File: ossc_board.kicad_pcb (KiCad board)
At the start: 2 copper layers, 124.6 x 68.7 mm, 173 parts, among them J1 VGA, J10 CLK9, J11 CLK8, J12 CLK2, J13 SD_CLK, J21 I2C_BCK, J22 I2C_WS, J23 I2C_DATA, J24 I2C_MCLK, J4 HDMI_CONN, J5 5VDC_IN, P1 JTAG_CONN, SW1 SPST, SW2 SW_PUSH, SW3 SW_PUSH, U1 TVP7002PZP, U10 S25FL216K, U12 TLV70012, U13 TLV70025, U14 TLV70012, U15 TLV70018, U16 TLV70018, U2 EP4CE15E22, U3 IT6613, U4 SN74LVC2G17, U5 AP7361C, U6 TLV70033, U7 NCP703SN19T1G, U9 TLV70019, Y1 ACHL-27MHZ-EK

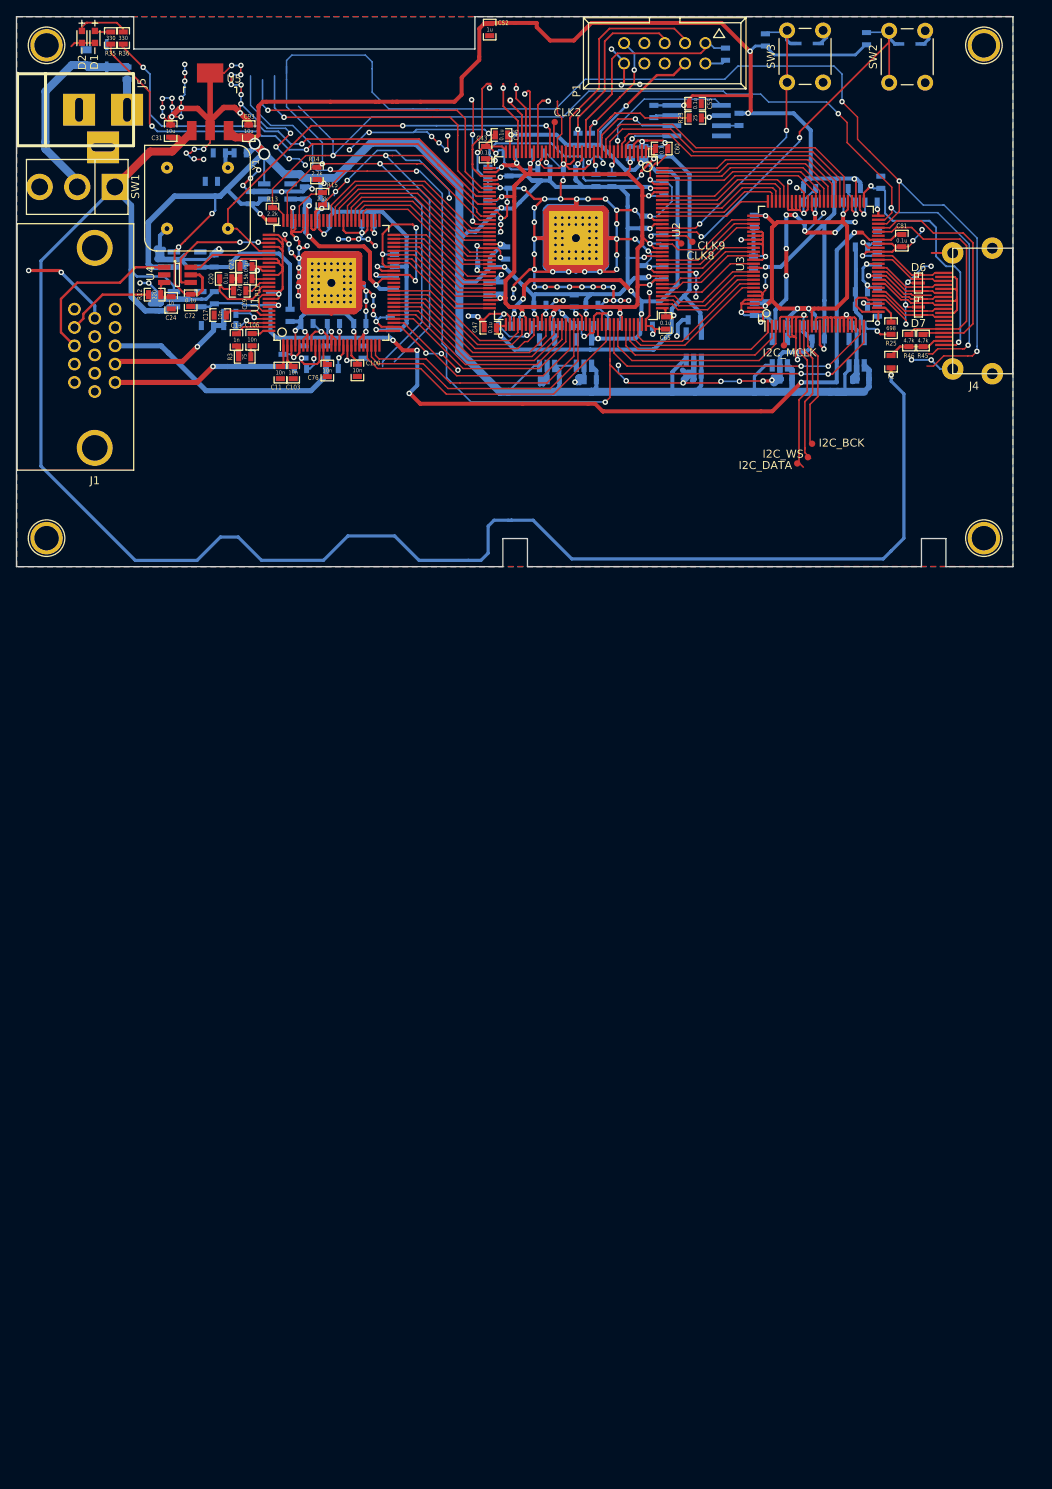
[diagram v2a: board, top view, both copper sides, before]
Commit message: NeXT Sound Box function (1st rev) (#1)
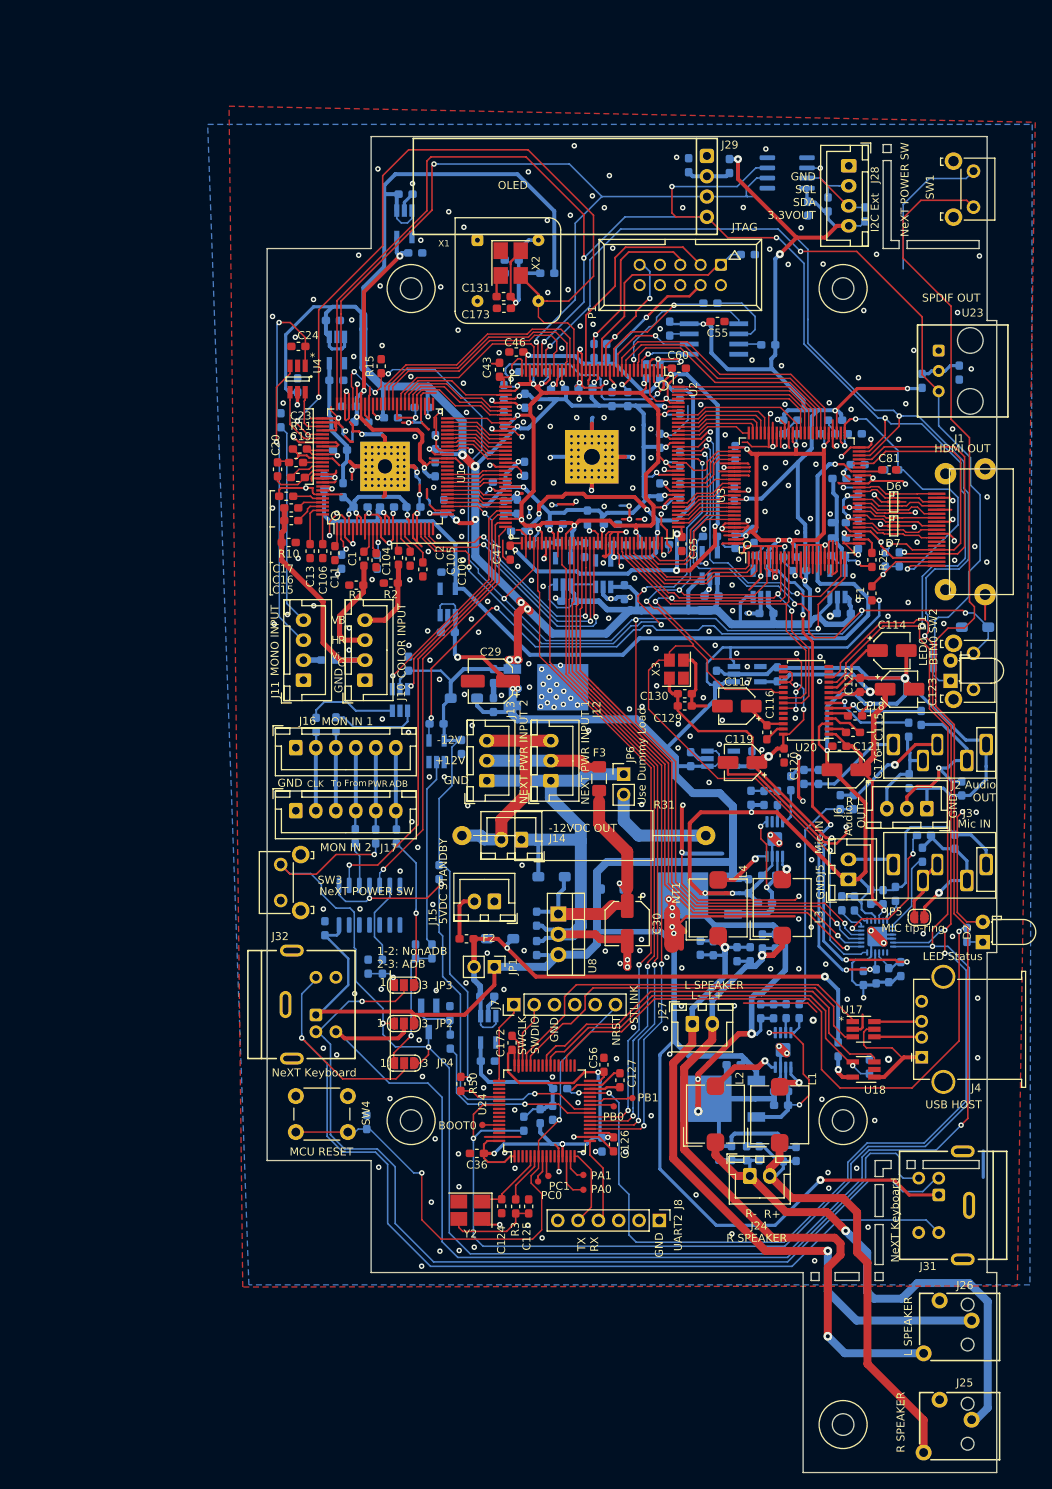
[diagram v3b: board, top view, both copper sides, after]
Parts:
- removed Y1: ACHL-27MHZ-EK, custom_components:ACHL-OSC
- added C102: 1u, Capacitor_SMD:C_0603_1608Metric_Pad1.05x0.95mm_HandSolder, B.Cu at (94.9, 99.7)
- added C111: 1u, Capacitor_SMD:C_0603_1608Metric_Pad1.05x0.95mm_HandSolder, B.Cu at (102.5, 99.2)
- added C112: 2200p (GRM1885C1H222JA01J), Capacitor_SMD:C_0603_1608Metric_Pad1.05x0.95mm_HandSolder, B.Cu at (125.5, 113.5)
- added C113: 2200p, Capacitor_SMD:C_0603_1608Metric_Pad1.05x0.95mm_HandSolder, B.Cu at (119.0, 112.6)
- added C114: 10u 16V, Capacitor_SMD:CP_Elec_4x4.5, F.Cu at (116.8, 96.3)
- added C115: 2.2u (GRM188R71A225KE15D), Capacitor_SMD:C_0603_1608Metric_Pad1.05x0.95mm_HandSolder, F.Cu at (111.9, 106.5)
- added C116: 0.1u, Capacitor_SMD:C_0603_1608Metric_Pad1.05x0.95mm_HandSolder, F.Cu at (101.2, 106.5)
- added C117: 10u 16V, Capacitor_SMD:CP_Elec_4x4.5, F.Cu at (97.4, 103.2)
- added C118: 2.2u, Capacitor_SMD:C_0603_1608Metric_Pad1.05x0.95mm_HandSolder, F.Cu at (112.2, 104.4)
- added C119: 10u 16V, Capacitor_SMD:CP_Elec_4x4.5, F.Cu at (98.1, 110.2)
- added C12: 1u, Capacitor_SMD:C_0603_1608Metric_Pad1.05x0.95mm_HandSolder, B.Cu at (125.2, 61.5)
- added C120: 0.1u, Capacitor_SMD:C_0603_1608Metric_Pad1.05x0.95mm_HandSolder, F.Cu at (103.3, 109.4)
- added C121: 0.1u, Capacitor_SMD:C_0603_1608Metric_Pad1.05x0.95mm_HandSolder, F.Cu at (110.2, 108.2)
- added C122: 0.1u, Capacitor_SMD:C_0603_1608Metric_Pad1.05x0.95mm_HandSolder, F.Cu at (112.8, 100.6)
- added C123: 10u 16V EEE-FK1C100AR or HB Series, Capacitor_SMD:CP_Elec_4x4.5, F.Cu at (117.8, 101.1)
- added C124: 10p, Capacitor_SMD:C_0603_1608Metric_Pad1.05x0.95mm_HandSolder, F.Cu at (68.0, 165.7)
- added C125: 10p, Capacitor_SMD:C_0603_1608Metric_Pad1.05x0.95mm_HandSolder, F.Cu at (71.4, 165.7)
- added C126: 0.01u, Capacitor_SMD:C_0603_1608Metric_Pad1.05x0.95mm_HandSolder, F.Cu at (82.0, 158.0)
- added C127: 2.2u, Capacitor_SMD:C_0603_1608Metric_Pad1.05x0.95mm_HandSolder, F.Cu at (82.8, 150.0)
- added C128: 0.1u, Capacitor_SMD:C_0603_1608Metric_Pad1.05x0.95mm_HandSolder, B.Cu at (51.2, 155.2)
- added C129: 1u, Capacitor_SMD:C_0603_1608Metric_Pad1.05x0.95mm_HandSolder, F.Cu at (90.9, 103.2)
- added C130: 0.01u, Capacitor_SMD:C_0603_1608Metric_Pad1.05x0.95mm_HandSolder, F.Cu at (90.9, 101.7)
- added C131: 0.01u, Capacitor_SMD:C_0603_1608Metric_Pad1.05x0.95mm_HandSolder, F.Cu at (68.3, 52.0)
- added C132: 0.1u, Capacitor_SMD:C_0603_1608Metric_Pad1.05x0.95mm_HandSolder, B.Cu at (63.0, 108.3)
- added C133: 0.1u, Capacitor_SMD:C_0603_1608Metric_Pad1.05x0.95mm_HandSolder, B.Cu at (45.9, 131.0)
- added C134: 0.1u, Capacitor_SMD:C_0603_1608Metric_Pad1.05x0.95mm_HandSolder, B.Cu at (116.4, 136.8)
- added C135: 0.1u, Capacitor_SMD:C_0603_1608Metric_Pad1.05x0.95mm_HandSolder, B.Cu at (115.7, 127.1)
- added C136: 1u, Capacitor_SMD:C_0603_1608Metric_Pad1.05x0.95mm_HandSolder, B.Cu at (114.2, 127.0)
- added C137: 0.1u, Capacitor_SMD:C_0603_1608Metric_Pad1.05x0.95mm_HandSolder, B.Cu at (113.2, 137.2)
- added C138: 1u, Capacitor_SMD:C_0603_1608Metric_Pad1.05x0.95mm_HandSolder, B.Cu at (114.8, 137.0)
- added C139: 1u, Capacitor_SMD:C_0603_1608Metric_Pad1.05x0.95mm_HandSolder, B.Cu at (120.6, 121.8)
- added C140: 1u, Capacitor_SMD:C_0603_1608Metric_Pad1.05x0.95mm_HandSolder, B.Cu at (117.2, 126.7)
- added C141: 1u, Capacitor_SMD:C_0603_1608Metric_Pad1.05x0.95mm_HandSolder, B.Cu at (124.7, 120.1)
- added C142: 0.1u, Capacitor_SMD:C_0603_1608Metric_Pad1.05x0.95mm_HandSolder, B.Cu at (112.1, 127.9)
- added C143: 0.1u, Capacitor_SMD:C_0603_1608Metric_Pad1.05x0.95mm_HandSolder, B.Cu at (110.5, 127.8)
- added C144: (220p), Capacitor_SMD:C_0603_1608Metric_Pad1.05x0.95mm_HandSolder, B.Cu at (57.3, 133.9)
- added C145: (220p), Capacitor_SMD:C_0603_1608Metric_Pad1.05x0.95mm_HandSolder, B.Cu at (51.3, 135.8)
- added C146: 2.2u, Capacitor_SMD:C_0603_1608Metric_Pad1.05x0.95mm_HandSolder, B.Cu at (102.9, 153.1)
- added C147: 1u, Capacitor_SMD:C_0603_1608Metric_Pad1.05x0.95mm_HandSolder, B.Cu at (98.9, 125.7)
- added C148: 0.1u, Capacitor_SMD:C_0603_1608Metric_Pad1.05x0.95mm_HandSolder, B.Cu at (102.9, 151.4)
- added C149: 2.2u, Capacitor_SMD:C_0603_1608Metric_Pad1.05x0.95mm_HandSolder, B.Cu at (112.0, 115.2)
- added C150: 0.1u, Capacitor_SMD:C_0603_1608Metric_Pad1.05x0.95mm_HandSolder, B.Cu at (110.4, 115.2)
- added C151: 0.1u, Capacitor_SMD:C_0603_1608Metric_Pad1.05x0.95mm_HandSolder, B.Cu at (103.2, 159.2)
- added C152: 1u, Capacitor_SMD:C_0603_1608Metric_Pad1.05x0.95mm_HandSolder, B.Cu at (104.8, 159.2)
- added C153: 0.1u, Capacitor_SMD:C_0603_1608Metric_Pad1.05x0.95mm_HandSolder, B.Cu at (102.0, 141.3)
- added C154: 0.1u, Capacitor_SMD:C_0603_1608Metric_Pad1.05x0.95mm_HandSolder, B.Cu at (96.7, 159.1)
- added C155: 1u, Capacitor_SMD:C_0603_1608Metric_Pad1.05x0.95mm_HandSolder, B.Cu at (95.2, 159.0)
- added C156: 1u, Capacitor_SMD:C_0603_1608Metric_Pad1.05x0.95mm_HandSolder, B.Cu at (100.2, 159.1)
- added C157: 2.2u, Capacitor_SMD:C_0603_1608Metric_Pad1.05x0.95mm_HandSolder, B.Cu at (100.4, 141.3)
- added C158: 0.1u, Capacitor_SMD:C_0603_1608Metric_Pad1.05x0.95mm_HandSolder, B.Cu at (98.6, 159.1)
- added C159: 2.2u, Capacitor_SMD:C_0603_1608Metric_Pad1.05x0.95mm_HandSolder, B.Cu at (101.5, 124.4)
- added C160: 1u, Capacitor_SMD:C_0603_1608Metric_Pad1.05x0.95mm_HandSolder, B.Cu at (97.0, 148.0)
- added C161: 0.1u, Capacitor_SMD:C_0603_1608Metric_Pad1.05x0.95mm_HandSolder, B.Cu at (100.9, 127.8)
- added C162: 2.2u, Capacitor_SMD:C_0603_1608Metric_Pad1.05x0.95mm_HandSolder, B.Cu at (107.6, 112.0)
- added C163: 0.1u, Capacitor_SMD:C_0603_1608Metric_Pad1.05x0.95mm_HandSolder, B.Cu at (105.8, 112.0)
- added C164: 0.1u, Capacitor_SMD:C_0603_1608Metric_Pad1.05x0.95mm_HandSolder, B.Cu at (100.6, 132.6)
- added C165: 1u, Capacitor_SMD:C_0603_1608Metric_Pad1.05x0.95mm_HandSolder, B.Cu at (102.3, 132.6)
- added C166: 0.1u, Capacitor_SMD:C_0603_1608Metric_Pad1.05x0.95mm_HandSolder, B.Cu at (100.8, 114.7)
- added C167: 0.1u, Capacitor_SMD:C_0603_1608Metric_Pad1.05x0.95mm_HandSolder, B.Cu at (92.8, 133.4)
- added C168: 1u, Capacitor_SMD:C_0603_1608Metric_Pad1.05x0.95mm_HandSolder, B.Cu at (94.5, 133.5)
- added C169: 1u, Capacitor_SMD:C_0603_1608Metric_Pad1.05x0.95mm_HandSolder, B.Cu at (97.4, 134.2)
- added C170: 2.2u, Capacitor_SMD:C_0603_1608Metric_Pad1.05x0.95mm_HandSolder, B.Cu at (99.2, 114.7)
- added C171: 0.1u, Capacitor_SMD:C_0603_1608Metric_Pad1.05x0.95mm_HandSolder, B.Cu at (99.1, 134.2)
- added C172: 0.1u, Capacitor_SMD:C_0603_1608Metric_Pad1.05x0.95mm_HandSolder, F.Cu at (69.3, 145.3)
- added C173: 1u, Capacitor_SMD:C_0603_1608Metric_Pad1.05x0.95mm_HandSolder, F.Cu at (68.3, 53.5)
- added C174: 0.1u, Capacitor_SMD:C_0603_1608Metric_Pad1.05x0.95mm_HandSolder, B.Cu at (106.3, 41.0)
- added C175: 0.1u, Capacitor_SMD:C_0603_1608Metric_Pad1.05x0.95mm_HandSolder, B.Cu at (91.4, 35.6)
- added C176: 10u 16V, Capacitor_SMD:CP_Elec_4x4.5, F.Cu at (111.1, 111.2)
- added C29: 47u, Capacitor_SMD:CP_Elec_5x5.3, F.Cu at (66.6, 100.1)
- added C3: 1u (GRT188R61H105KE13D), Capacitor_SMD:C_0603_1608Metric_Pad1.05x0.95mm_HandSolder, B.Cu at (66.2, 139.5)
- added C30: 47u (EEE-HBC470UAR), Capacitor_SMD:CP_Elec_5x5.3, F.Cu at (83.7, 130.4)
- added C36: 0.01u, Capacitor_SMD:C_0603_1608Metric_Pad1.05x0.95mm_HandSolder, F.Cu at (64.9, 159.1)
- added C4: 1u, Capacitor_SMD:C_0603_1608Metric_Pad1.05x0.95mm_HandSolder, B.Cu at (66.3, 147.6)
- added C5: 1u, Capacitor_SMD:C_0603_1608Metric_Pad1.05x0.95mm_HandSolder, B.Cu at (72.4, 129.8)
- added C56: 0.1u, Capacitor_SMD:C_0603_1608Metric_Pad1.05x0.95mm_HandSolder, F.Cu at (80.8, 148.0)
- added C6: 1u, Capacitor_SMD:C_0603_1608Metric_Pad1.05x0.95mm_HandSolder, B.Cu at (72.4, 133.4)
- added C7: 0.1u, Capacitor_SMD:C_0603_1608Metric_Pad1.05x0.95mm_HandSolder, B.Cu at (56.4, 97.9)
- added C70: 1u, Capacitor_SMD:C_0603_1608Metric_Pad1.05x0.95mm_HandSolder, B.Cu at (91.6, 109.8)
- added C71: 1u, Capacitor_SMD:C_0603_1608Metric_Pad1.05x0.95mm_HandSolder, B.Cu at (99.3, 109.7)
- added D8: RB160M-30TR, custom_components:D_SOD-123_HandSoldering, B.Cu at (67.8, 132.3)
- added D9: (RB160M-30TR), custom_components:D_SOD-123_HandSoldering, B.Cu at (81.8, 126.1)
- added F3: 1A 1206 size (C1F 1), Fuse:Fuse_1206_3216Metric_Pad1.42x1.75mm_HandSolder, F.Cu at (80.2, 112.3)
- added FB10: MPZ1608S221A, Inductor_SMD:L_0603_1608Metric_Pad1.05x0.95mm_HandSolder, B.Cu at (96.5, 35.7)
- added FB3: MPZ1608S221A, Inductor_SMD:L_0603_1608Metric_Pad1.05x0.95mm_HandSolder, B.Cu at (72.8, 154.5)
- added FB8: MPZ1608S221A, Inductor_SMD:L_0603_1608Metric_Pad1.05x0.95mm_HandSolder, B.Cu at (110.1, 146.1)
- added FB9: MPZ1608S221A, Inductor_SMD:L_0603_1608Metric_Pad1.05x0.95mm_HandSolder, B.Cu at (120.6, 62.5)
- added J14: -12VDC OUT, Connector_JST:JST_XH_B2B-XH-A_1x02_P2.50mm_Vertical, F.Cu at (70.5, 119.9)
- added J15: 5VDC STANDBY, Connector_JST:JST_XH_B2B-XH-A_1x02_P2.50mm_Vertical, F.Cu at (67.1, 127.6)
- added J16: MON IN 1, Connector_JST:JST_XH_B6B-XH-A_1x06_P2.50mm_Vertical, F.Cu at (42.3, 108.4)
- added J17: MON IN 2, Connector_JST:JST_XH_B6B-XH-A_1x06_P2.50mm_Vertical, F.Cu at (42.3, 116.3)
- added J18: PA1, custom_components:TestPad-D1.0mm, F.Cu at (78.2, 161.8)
- added J19: BOOT0, custom_components:TestPad-D1.0mm, F.Cu at (65.6, 155.5)
- added J2: OUT (SJ1-3535NG), custom_components:SJ1-3535NG, F.Cu at (128.6, 108.9)
- added J20: PC0, custom_components:TestPad-D1.0mm, F.Cu at (72.6, 162.6)
- added J25: R SPEAKER (SJ-2509N), custom_components:SJ-2509N, F.Cu at (130.3, 192.4)
- added J26: L SPEAKER, custom_components:SJ-2509N, F.Cu at (130.3, 180.0)
- added J27: L SPK, Connector_JST:JST_XH_B2B-XH-A_1x02_P2.50mm_Vertical, F.Cu at (91.8, 142.9)
- added J28: I2C Ext, Connector_JST:JST_XH_B4B-XH-A_1x04_P2.50mm_Vertical, F.Cu at (111.4, 35.7)
- added J29: OLED, custom_components:OLED_0.91inch_I2C, F.Cu at (93.7, 34.4)
- added J3: MIC (SJ1-3535NG), custom_components:SJ1-3535NG, F.Cu at (128.6, 123.9)
- added J31: NeXT Keyboard, custom_components:Mini_DIN_5P, F.Cu at (131.2, 165.6)
- added J32: NeXT Keyboard (MD-50SM / KMDGX-5S-BS), custom_components:Mini_DIN_5P, F.Cu at (36.3, 140.5)
- added J6: Audio OUT, Connector_JST:JST_XH_B3B-XH-A_1x03_P2.50mm_Vertical, F.Cu at (121.2, 116.0)
- added J7: STLINK, Connector_PinHeader_2.54mm:PinHeader_1x06_P2.54mm_Vertical, F.Cu at (69.5, 140.5)
- added J8: UART2, Connector_PinHeader_2.54mm:PinHeader_1x06_P2.54mm_Vertical, F.Cu at (87.7, 167.5)
- added J9: PA0, custom_components:TestPad-D1.0mm, F.Cu at (78.2, 163.7)
- added JP1: Standby DC From NeXT Hardware, Connector_PinHeader_2.54mm:PinHeader_1x02_P2.54mm_Vertical, F.Cu at (67.1, 135.8)
- added JP2: KBD_SW, Jumper:SolderJumper-3_P1.3mm_Open_RoundedPad1.0x1.5mm_NumberLabels, F.Cu at (55.8, 142.9)
- added JP3: KBD_SW, Jumper:SolderJumper-3_P1.3mm_Open_RoundedPad1.0x1.5mm_NumberLabels, F.Cu at (55.8, 138.1)
- added JP4: KBD_SW, Jumper:SolderJumper-3_P1.3mm_Open_RoundedPad1.0x1.5mm_NumberLabels, F.Cu at (55.8, 147.8)
- added JP5: MIC tip-ring, Jumper:SolderJumper-2_P1.3mm_Open_RoundedPad1.0x1.5mm, F.Cu at (120.2, 129.6)
- added JP6: Use Dummy Load, Connector_PinHeader_2.54mm:PinHeader_1x02_P2.54mm_Vertical, F.Cu at (83.3, 111.7)
- added L1: 33uH (SLF7045T-330MR), custom_components:L_TDK_SLF7045_HandSoldering, F.Cu at (102.8, 154.3)
- added L2: 33uH, custom_components:L_TDK_SLF7045_HandSoldering, F.Cu at (94.7, 154.2)
- added L3: 33uH, custom_components:L_TDK_SLF7045_HandSoldering, F.Cu at (103.1, 128.4)
- added L4: 33uH, custom_components:L_TDK_SLF7045_HandSoldering, F.Cu at (95.1, 128.4)
- added MH5: CONN_1, MountingHole:MountingHole_2.7mm_M2.5, F.Cu at (110.7, 193.0)
- added NT1: AGND_DGND, NetTie:NetTie-2_SMD_Pad2.0mm, F.Cu at (89.3, 131.0)
- added Q1: 2SC2712, Package_TO_SOT_SMD:SC-59_Handsoldering, B.Cu at (58.9, 142.3)
- added R27: 470, Resistor_SMD:R_0603_1608Metric_Pad1.05x0.95mm_HandSolder, B.Cu at (120.5, 104.7)
- added R28: 470, Resistor_SMD:R_0603_1608Metric_Pad1.05x0.95mm_HandSolder, B.Cu at (118.9, 106.1)
- added R29: 10k, Resistor_SMD:R_0603_1608Metric_Pad1.05x0.95mm_HandSolder, B.Cu at (59.3, 133.9)
- added R30: 1k, Resistor_SMD:R_0603_1608Metric_Pad1.05x0.95mm_HandSolder, B.Cu at (53.1, 135.8)
- added R31: 2x 100 5W (or 47ohm 7W), Resistor_THT:R_Axial_DIN0617_L17.0mm_D6.0mm_P30.48mm_Horizontal, F.Cu at (63.1, 119.4)
- added R32: 1k, Resistor_SMD:R_0603_1608Metric_Pad1.05x0.95mm_HandSolder, B.Cu at (126.2, 131.8)
- added R33: (47k), Resistor_SMD:R_0603_1608Metric_Pad1.05x0.95mm_HandSolder, B.Cu at (74.4, 154.0)
- added R34: 4.7k, Resistor_SMD:R_0603_1608Metric_Pad1.05x0.95mm_HandSolder, B.Cu at (61.6, 145.1)
- added R37: 47k, Resistor_SMD:R_0603_1608Metric_Pad1.05x0.95mm_HandSolder, B.Cu at (60.2, 124.0)
- added R38: 2.2k, Resistor_SMD:R_0603_1608Metric_Pad1.05x0.95mm_HandSolder, B.Cu at (120.8, 119.4)
- added R39: 100k, Resistor_SMD:R_0603_1608Metric_Pad1.05x0.95mm_HandSolder, B.Cu at (105.2, 141.3)
- added R4: 22, Resistor_SMD:R_0603_1608Metric_Pad1.05x0.95mm_HandSolder, B.Cu at (54.9, 119.5)
- added R40: 100k, Resistor_SMD:R_0603_1608Metric_Pad1.05x0.95mm_HandSolder, B.Cu at (103.6, 141.3)
- added R44: 100k, Resistor_SMD:R_0603_1608Metric_Pad1.05x0.95mm_HandSolder, B.Cu at (102.5, 114.7)
- added R47: 10k, Resistor_SMD:R_0603_1608Metric_Pad1.05x0.95mm_HandSolder, B.Cu at (108.8, 40.5)
- added R48: 10k, Resistor_SMD:R_0603_1608Metric_Pad1.05x0.95mm_HandSolder, B.Cu at (113.4, 41.7)
- added R49: 22-150, Resistor_SMD:R_0603_1608Metric_Pad1.05x0.95mm_HandSolder, B.Cu at (46.4, 97.4)
- added R5: 330, Resistor_SMD:R_0603_1608Metric_Pad1.05x0.95mm_HandSolder, B.Cu at (52.3, 119.5)
- added R50: 10k, Resistor_SMD:R_0603_1608Metric_Pad1.05x0.95mm_HandSolder, F.Cu at (62.9, 150.4)
- added R6: 100, Resistor_SMD:R_0603_1608Metric_Pad1.05x0.95mm_HandSolder, B.Cu at (44.8, 105.5)
- added R7: 100, Resistor_SMD:R_0603_1608Metric_Pad1.05x0.95mm_HandSolder, B.Cu at (47.3, 105.5)
- added R8: 22, Resistor_SMD:R_0603_1608Metric_Pad1.05x0.95mm_HandSolder, B.Cu at (49.7, 119.4)
- added R9: 47k, Resistor_SMD:R_0603_1608Metric_Pad1.05x0.95mm_HandSolder, B.Cu at (114.0, 148.3)
- added SW4: MCU RESET, Button_Switch_THT:SW_PUSH_6mm, F.Cu at (42.3, 151.9)
- added U11: TLV70033DDCR, custom_components:SOT-23-5_Handsoldering, B.Cu at (66.3, 143.6)
- added U17: USBLC6-2SC6, Package_TO_SOT_SMD:SOT-23-6_Handsoldering, F.Cu at (113.3, 143.6)
- added U18: STMPS2151STR‎ or TPS2051CDBV, Package_TO_SOT_SMD:SOT-23-5_HandSoldering, F.Cu at (113.3, 148.6)
- added U19: SN74LVC2G34DBV, Package_TO_SOT_SMD:SOT-23-6_Handsoldering, B.Cu at (55.3, 102.4)
- added U20: PCM5122PW, Package_SO:TSSOP-28_4.4x9.7mm_P0.65mm, F.Cu at (106.1, 102.5)
- added U21: TLV70033DDCR (or XC6204B332MR-G), custom_components:SOT-23-5_Handsoldering, B.Cu at (95.4, 109.8)
- added U22: TLV70033DDCR (or XC6204B332MR-G), custom_components:SOT-23-5_Handsoldering, B.Cu at (98.7, 99.2)
- added U23: PLT133/T, custom_components:PLT133_T, F.Cu at (131.3, 61.3)
- added U24: STM32F401RCT6, Package_QFP:LQFP-64_10x10mm_P0.5mm, F.Cu at (73.4, 153.8)
- added U25: SN74LVC1G07DBV, Package_TO_SOT_SMD:SOT-23-5_HandSoldering, B.Cu at (59.9, 108.8)
- added U26: SN74HCT125DR, Package_SO:SOIC-14_3.9x8.7mm_P1.27mm, B.Cu at (51.5, 128.1)
- added U27: TLV320ADC3100, Package_DFN_QFN:VQFN-24-1EP_4x4mm_P0.5mm_EP2.45x2.45mm, B.Cu at (115.0, 132.0)
- added U28: BD33FC0FP, Package_TO_SOT_SMD:TO-252-2, B.Cu at (95.7, 152.3)
- added U29: TPA2005D1DGN, Package_SO:MSOP-8-1EP_3x3mm_P0.65mm_EP1.73x1.85mm, B.Cu at (103.2, 146.2)
- added U30: BD33FC0FP, Package_TO_SOT_SMD:TO-252-2, B.Cu at (92.7, 126.9)
- added U31: TPA2005D1DGN, Package_SO:MSOP-8-1EP_3x3mm_P0.65mm_EP1.73x1.85mm, B.Cu at (102.2, 119.8)
- added U32: PCA9515AD, Package_SO:SOIC-8_3.9x4.9mm_P1.27mm, B.Cu at (103.7, 36.6)
- added U8: 5V(DC/DC), Package_TO_SOT_THT:TO-220-3_Vertical, F.Cu at (75.1, 129.2)
- added X1: ACHL-27MHZ-EK, custom_components:ACHL-OSC, F.Cu at (68.8, 48.8)
- added X2: ASEDV-27.000MHZ-LR-T(ECS-2333-270-BN-TR), Oscillator:Oscillator_SMD_SeikoEpson_SG8002CE-4Pin_3.2x2.5mm_HandSoldering, F.Cu at (69.2, 47.8)
- added X3: ECS-2520MVLC-225.792-BN-TR, Oscillator:Oscillator_SMD_SeikoEpson_SG210-4Pin_2.5x2.0mm_HandSoldering, F.Cu at (89.9, 98.6)
- added Y2: 25MHz (FA-238 25.0000MB-K0), Crystal:Crystal_SMD_SeikoEpson_TSX3225-4Pin_3.2x2.5mm_HandSoldering, F.Cu at (64.1, 166.2)
- C1, C15, C2: footprint custom_components:SM0603_Capa_libcms -> Capacitor_SMD:C_0603_1608Metric_Pad1.05x0.95mm_HandSolder; moved to F.Cu
- C10, C101, C108, C109, C110, C14, C18, C20, C21, C22, C23, C26, C27, C28, C32, C33, C34, C35, C37, C38, C39, C40, C41, C42, C43, C44, C45, C46, C47, C48, C49, C50, C51, C53, C54, C55, C57, C58, C59, C60, C61, C62, C63, C64, C65, C66, C67, C68, C69, C73, C74, C75, C77, C78, C79, C8, C80, C81, C82, C83, C84, C85, C86, C87, C88, C89, C9, C90, C91, C92, C94, C95, C96, C97, C98, C99: footprint custom_components:SM0603_Capa_libcms -> Capacitor_SMD:C_0603_1608Metric_Pad1.05x0.95mm_HandSolder
- C100, C106, C17, C25: value 10n -> 0.01u; footprint custom_components:SM0603_Capa_libcms -> Capacitor_SMD:C_0603_1608Metric_Pad1.05x0.95mm_HandSolder
- C103, C76: value 10n -> 0.01u; footprint custom_components:SM0603_Capa_libcms -> Capacitor_SMD:C_0603_1608Metric_Pad1.05x0.95mm_HandSolder; moved to B.Cu
- C104, C105: value 10n -> 0.01u; footprint custom_components:SM0603_Capa_libcms -> Capacitor_SMD:C_0603_1608Metric_Pad1.05x0.95mm_HandSolder; moved to F.Cu
- C107: value 47u -> 2.2u; footprint custom_components:SM0805_libcms -> Capacitor_SMD:C_0603_1608Metric_Pad1.05x0.95mm_HandSolder
- C11: value 10n -> 0.01u (GCM188R72A103KA37J); footprint custom_components:SM0603_Capa_libcms -> Capacitor_SMD:C_0603_1608Metric_Pad1.05x0.95mm_HandSolder
- C13, C24: value 1n -> 1000p; footprint custom_components:SM0603_Capa_libcms -> Capacitor_SMD:C_0603_1608Metric_Pad1.05x0.95mm_HandSolder
- C16: value 1n -> 1000p; footprint custom_components:SM0603_Capa_libcms -> Capacitor_SMD:C_0603_1608Metric_Pad1.05x0.95mm_HandSolder; moved to F.Cu
- C19: value 4.7n -> 4700p; footprint custom_components:SM0603_Capa_libcms -> Capacitor_SMD:C_0603_1608Metric_Pad1.05x0.95mm_HandSolder
- C31: value 10u -> 10u (ZRB18AR61E106ME01L); footprint custom_components:SM0603_Capa_libcms -> Capacitor_SMD:C_0603_1608Metric_Pad1.05x0.95mm_HandSolder; moved to B.Cu
- C52, C72, C93: footprint custom_components:SM0603_Capa_libcms -> Capacitor_SMD:C_0603_1608Metric_Pad1.05x0.95mm_HandSolder; moved to B.Cu
- D1: value LEDR -> LED0; footprint custom_components:LED-0603 -> LED_THT:LED_D3.0mm_Horizontal_O1.27mm_Z6.0mm
- D2: value LEDG -> LED Status; footprint custom_components:LED-0603 -> LED_THT:LED_D3.0mm_Horizontal_O1.27mm_Z6.0mm
- D3, D4, D5: value SD05-7 -> RB160M-30TR; footprint custom_components:SOD-323_Handsoldering -> custom_components:D_SOD-123_HandSoldering
- D6, D7: value RClamp0524P -> RCLAMP0524PATCT
- F1: value F0603E1R50FSTR -> MF-FSMF020X-2; footprint custom_components:SM0603_Resistor_libcms -> Inductor_SMD:L_0603_1608Metric_Pad1.05x0.95mm_HandSolder; moved to F.Cu
- F2: value MF-FSMF020X-2 -> 0.5A 0603 size (ERB-RE0R50V); footprint custom_components:SM0603_Resistor_libcms -> Fuse:Fuse_0603_1608Metric_Pad1.05x0.95mm_HandSolder
- FB1, FB2, FB4, FB5, FB6, FB7: footprint custom_components:SM0603_Resistor_libcms -> Inductor_SMD:L_0603_1608Metric_Pad1.05x0.95mm_HandSolder
- J1: value VGA -> HDMI_CONN (10029449-111RLF); footprint custom_components:VGA_CONN -> custom_components:HDMI_CONN-10029449-111RLF
- J10: value CLK9 -> COLOR INPUT; footprint custom_components:TestPad-D1.0mm -> Connector_JST:JST_XH_B4B-XH-A_1x04_P2.50mm_Vertical
- J11: value CLK8 -> MONO INPUT; footprint custom_components:TestPad-D1.0mm -> Connector_JST:JST_XH_B4B-XH-A_1x04_P2.50mm_Vertical
- J12: value CLK2 -> NEXT PWR INPUT 1; footprint custom_components:TestPad-D1.0mm -> Connector_JST:JST_XH_B3B-XH-A_1x03_P2.50mm_Vertical
- J13: value SD_CLK -> NEXT PWR INPUT 2; footprint custom_components:TestPad-D1.0mm -> Connector_JST:JST_XH_B3B-XH-A_1x03_P2.50mm_Vertical
- J21: value I2C_BCK -> PC1
- J22: value I2C_WS -> PB0
- J23: value I2C_DATA -> PB1
- J24: value I2C_MCLK -> R SPK; footprint custom_components:TestPad-D1.0mm -> Connector_JST:JST_XH_B2B-XH-A_1x02_P2.50mm_Vertical
- J4: value HDMI_CONN -> USB Host (SS-52100-001); footprint custom_components:HDMI_CONN-10029449-111RLF -> Connector_USB:USB_A_Stewart_SS-52100-001_Horizontal
- J5: value 5VDC_IN -> Mic IN; footprint custom_components:BARREL_JACK_roundconn -> Connector_JST:JST_XH_B2B-XH-A_1x02_P2.50mm_Vertical
- MH1, MH2, MH3, MH4: footprint Connect:1pin -> MountingHole:MountingHole_2.7mm_M2.5
- P1: value JTAG_CONN -> JTAG (30310-6002HB)
- R1, R10, R2: footprint custom_components:SM0603_Resistor_libcms -> Resistor_SMD:R_0603_1608Metric_Pad1.05x0.95mm_HandSolder; moved to F.Cu
- R11, R16, R17, R18, R19, R20, R21, R22, R24, R26, R41, R42: footprint custom_components:SM0603_Resistor_libcms -> Resistor_SMD:R_0603_1608Metric_Pad1.05x0.95mm_HandSolder
- R12, R13, R14, R45, R46: footprint custom_components:SM0603_Resistor_libcms -> Resistor_SMD:R_0603_1608Metric_Pad1.05x0.95mm_HandSolder; moved to B.Cu
- R15: value 2.2k -> 10k; footprint custom_components:SM0603_Resistor_libcms -> Resistor_SMD:R_0603_1608Metric_Pad1.05x0.95mm_HandSolder
- R23: value 25 -> 22; footprint custom_components:SM0603_Resistor_libcms -> Resistor_SMD:R_0603_1608Metric_Pad1.05x0.95mm_HandSolder; moved to B.Cu
- R25: value 698 -> 698 1%; footprint custom_components:SM0603_Resistor_libcms -> Resistor_SMD:R_0603_1608Metric_Pad1.05x0.95mm_HandSolder
- R3: value 75 -> 1k; footprint custom_components:SM0603_Resistor_libcms -> Resistor_SMD:R_0603_1608Metric_Pad1.05x0.95mm_HandSolder
- R35: value 330 -> 1k; footprint custom_components:SM0603_Resistor_libcms -> Resistor_SMD:R_0603_1608Metric_Pad1.05x0.95mm_HandSolder; moved to B.Cu
- R36: value 330 -> 47k; footprint custom_components:SM0603_Resistor_libcms -> Resistor_SMD:R_0603_1608Metric_Pad1.05x0.95mm_HandSolder; moved to B.Cu
- R43: value 10k -> 100k; footprint custom_components:SM0603_Resistor_libcms -> Resistor_SMD:R_0603_1608Metric_Pad1.05x0.95mm_HandSolder
- SW1: value SPST -> NeXT POWER SW (1-1825027-1 / 2-1825027-0); footprint custom_components:SW_SPDT -> Button_Switch_THT:SW_Tactile_SKHH_Angled
- SW2: value SW_PUSH -> BTN0; footprint Button_Switch_THT:SW_PUSH_6mm_H5mm -> Button_Switch_THT:SW_Tactile_SKHH_Angled
- SW3: value SW_PUSH -> NeXT POWER SW; footprint Button_Switch_THT:SW_PUSH_6mm_H5mm -> Button_Switch_THT:SW_Tactile_SKHH_Angled
- U10: value S25FL216K -> S25FL216K (IS25LP016D-JBLE)
- U12, U14: value TLV70012 -> TLV70012DDCT
- U13: value TLV70025 -> TLV70025DDCT
- U15, U16: value TLV70018 -> TLV70018DDCT
- U2: value EP4CE15E22 -> EP4CE15E22C8N
- U3: value IT6613 -> IT6613E
- U4: value SN74LVC2G17 -> SN74LVC2G17DBV
- U5: value AP7361C -> BD33FC0FP; footprint custom_components:SOT-223_Handsoldering -> Package_TO_SOT_SMD:TO-252-2; moved to B.Cu
- U6: value TLV70033 -> TLV70033DDCR
- U9: value TLV70019 -> TLV70019DDCT
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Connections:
- net /fpga1/BTN0 renamed /fpga1/FromKBD
- C1 pad 1: /tvp_board1/RGB3_R -> /soundbox/RED_OUT
- C101 pad 1: /hdmitx1/DVDD3V3 -> VCC
- C108 pad 1: /hdmitx1/DVDD3V3 -> VCC
- C13 pad 1: /tvp_board1/RGB1_S -> GND
- C14 pad 1: /hdmitx1/DVDD3V3 -> VCC
- C15 pad 1: /tvp_board1/RGB3_G -> /soundbox/GREEN_OUT
- C16 pad 1: /tvp_board1/RGB3_G -> /soundbox/GREEN_OUT
- C2 pad 1: /tvp_board1/RGB3_B -> /soundbox/BLUE_OUT
- C22 pad 1: /hdmitx1/DVDD3V3 -> VCC
- C26 pad 1: /hdmitx1/DVDD3V3 -> VCC
- C28 pad 1: /hdmitx1/DVDD3V3 -> VCC
- C32 pad 2: /hdmitx1/DVDD3V3 -> VCC
- C34 pad 1: /hdmitx1/DVDD3V3 -> VCC
- C40 pad 1: /hdmitx1/DVDD3V3 -> VCC
- C45 pad 1: /hdmitx1/DVDD3V3 -> VCC
- C52 pad 1: /hdmitx1/DVDD3V3 -> /soundbox/A_DVDD
- C53 pad 1: /hdmitx1/DVDD3V3 -> VCC
- C55 pad 2: /hdmitx1/DVDD3V3 -> VCC
- C57 pad 1: /hdmitx1/DVDD3V3 -> VCC
- C62 pad 1: /hdmitx1/DVDD3V3 -> VCC
- C63 pad 1: /hdmitx1/DVDD3V3 -> VCC
- C72 pad 1: /hdmitx1/DVDD3V3 -> VCC
- C73 pad 1: /hdmitx1/DVDD3V3 -> VCC
- C79 pad 1: /hdmitx1/DVDD3V3 -> VCC
- C83 pad 1: /hdmitx1/DVDD3V3 -> VCC
- C86 pad 1: /hdmitx1/DVDD3V3 -> VCC
- C87 pad 1: /hdmitx1/DVDD3V3 -> VCC
- C88 pad 1: /hdmitx1/DVDD3V3 -> VCC
- C91 pad 1: /hdmitx1/DVDD3V3 -> VCC
- C92 pad 1: /hdmitx1/DVDD3V3 -> VCC
- C93 pad 1: /hdmitx1/DVDD3V3 -> VCC
- C94 pad 1: /hdmitx1/DVDD3V3 -> VCC
- C99 pad 1: /hdmitx1/DVDD3V3 -> VCC
- D4 pad 1: /fpga1/BTN1 -> /hdmitx1/5V
- D4 pad 2: GND -> VCC
- D5 pad 1: Net-(C107-Pad1) -> Net-(C30-Pad1)
- F1 pad 1: Net-(F1-Pad1) -> /hdmitx1/5V
- F1 pad 2: Net-(C107-Pad1) -> /hdmitx1/5V_FUSED
- F2 pad 1: /hdmitx1/5V -> Net-(F2-Pad1)
- F2 pad 2: /hdmitx1/5V_FUSED -> /soundbox/5VDC_STBY
- FB5 pad 2: /hdmitx1/DVDD3V3 -> VCC
- J1 pad 1: /tvp_board1/RGB3_R -> /hdmitx1/TMDS_D2+
- J1 pad 10: GND -> /hdmitx1/TMDS_CLK+
- J1 pad 11: Net-(J1-Pad11) -> GND
- J1 pad 12: Net-(J1-Pad12) -> /hdmitx1/TMDS_CLK-
- J1 pad 13: /tvp_board1/RGB3_HS -> Net-(J1-Pad13)
- J1 pad 14: /tvp_board1/RGB3_VS -> Net-(J1-Pad14)
- J1 pad 15: Net-(J1-Pad15) -> /hdmitx1/DDC_SCL
- J1 pad 2: /tvp_board1/RGB3_G -> GND
- J1 pad 3: /tvp_board1/RGB3_B -> /hdmitx1/TMDS_D2-
- J1 pad 4: Net-(J1-Pad4) -> /hdmitx1/TMDS_D1+
- J1 pad 6: GND -> /hdmitx1/TMDS_D1-
- J1 pad 7: GND -> /hdmitx1/TMDS_D0+
- J1 pad 9: Net-(J1-Pad9) -> /hdmitx1/TMDS_D0-
- J10 pad 1: Net-(J10-Pad1) -> GND
- J11 pad 1: Net-(J11-Pad1) -> GND
- J12 pad 1: Net-(J12-Pad1) -> GND
- J13 pad 1: Net-(J13-Pad1) -> GND
- J21 pad 1: /hdmitx1/I2S_BCK -> Net-(J21-Pad1)
- J22 pad 1: /hdmitx1/I2S_WS -> Net-(J22-Pad1)
- J23 pad 1: /hdmitx1/I2S_DATA -> Net-(J23-Pad1)
- J24 pad 1: Net-(J24-Pad1) -> /soundbox/R_SP_N
- J4 pad 1: /hdmitx1/TMDS_D2+ -> Net-(J4-Pad1)
- J4 pad 2: GND -> Net-(J4-Pad2)
- J4 pad 3: /hdmitx1/TMDS_D2- -> Net-(J4-Pad3)
- J4 pad 4: /hdmitx1/TMDS_D1+ -> GND
- J5 pad 1: Net-(F1-Pad1) -> GNDA
- J5 pad 2: GND -> Net-(J3-PadTN)
- R1 pad 1: /tvp_board1/RGB3_R -> /soundbox/RED_OUT
- R10 pad 2: /tvp_board1/RGB3_G -> /soundbox/GREEN_OUT
- R13 pad 1: /fpga1/SDA -> /soundbox/S_DVDD
- R13 pad 2: /hdmitx1/DVDD3V3 -> /fpga1/SDA
- R14 pad 1: /hdmitx1/DVDD3V3 -> /soundbox/S_DVDD
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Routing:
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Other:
- board size 124.6 x 68.7 mm -> 91.2 x 167 mm
- net class Default: clearance 0.16 -> 0.2; trace_width 0.22 -> 0.2
- net class FAT_power: clearance 0.16 -> 0.2
- net class Power: clearance 0.16 -> 0.2; via_drill 0.35 -> 0.4
- net class digi_hs: clearance 0.16 -> 0.2
- rule trace_clearance: 0.16 -> 0.2
- rule trace_min: 0.16 -> 0.18
- board text added: "*"
- board text added: "+12V"
- board text added: "-12V"
- board text added: "1-2: NonADB 2-3: ADB"
- board text added: "15mm"
- board text added: "27mm"
- board text added: "ADB"
- board text added: "Audio OUT"
- board text added: "B"
- board text added: "CLK"
- board text added: "Case(inner)"
- board text added: "Case(outer)"
- board text added: "Components safe area"
- board text added: "From"
- board text added: "G"
- board text added: "GND"
- board text added: "GND SCL SDA 3.3VOUT"
- board text added: "H"
- board text added: "HDMI OUT"
- board text added: "JTAG"
- board text added: "L SPEAKER"
- board text added: "L+"
- board text added: "L-"
- board text added: "Mic IN"
- board text added: "NRST"
- board text added: "NeXT Keyboard"
- board text added: "NeXT POWER SW"
- board text added: "PWR"
- board text added: "Panel(inner)"
- board text added: "Panel(outer) t1.5"
- board text added: "R"
- board text added: "R L"
- board text added: "R SPEAKER"
- board text added: "R+"
- board text added: "R-"
- board text added: "SPDIF OUT"
- board text added: "SWCLK"
- board text added: "SWDIO"
- board text added: "Sw(case+5mm)"
- board text added: "TX RX"
- board text added: "Tactile L=8.4mm or 11.3mm"
- board text added: "To"
- board text added: "USB HOST"
- board text added: "V"
- board text added: "Vi"

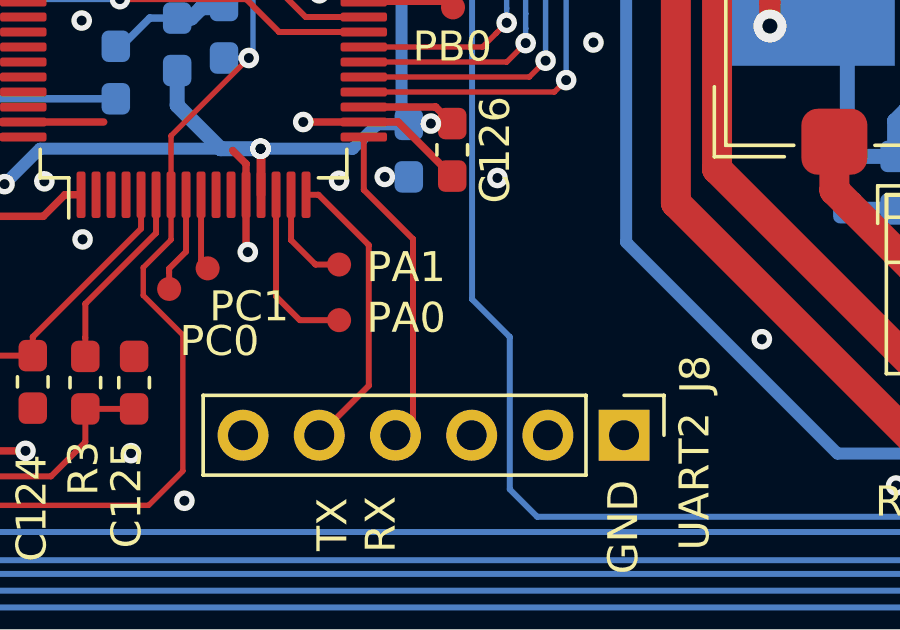
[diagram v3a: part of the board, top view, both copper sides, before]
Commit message: add uart registors
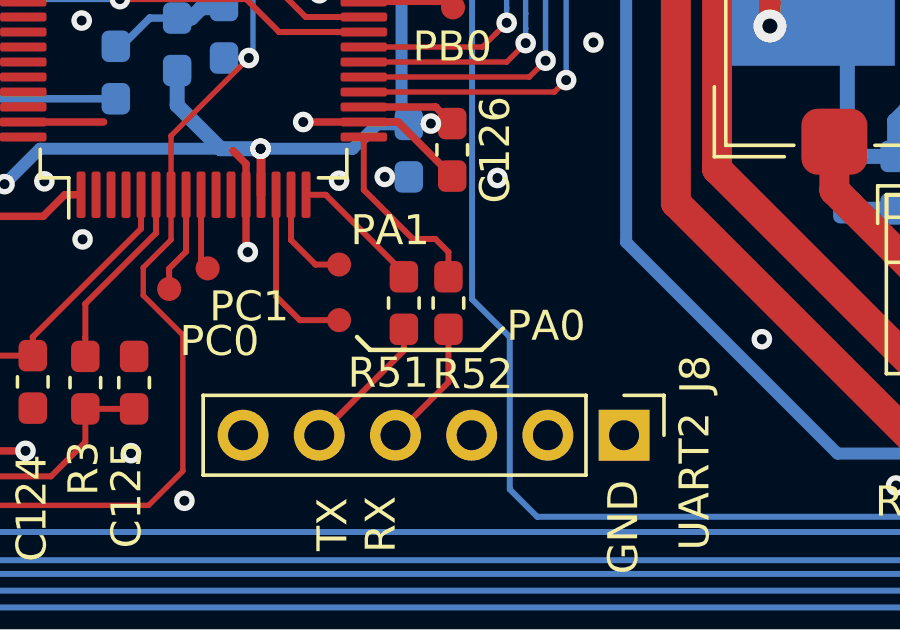
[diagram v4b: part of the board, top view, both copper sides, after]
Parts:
- added R51: 1k, Resistor_SMD:R_0603_1608Metric_Pad1.05x0.95mm_HandSolder, F.Cu at (80.4, 163.1)
- added R52: 1k, Resistor_SMD:R_0603_1608Metric_Pad1.05x0.95mm_HandSolder, F.Cu at (81.9, 163.1)
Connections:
- U24 pad 16: /soundbox/URT2_TX -> Net-(R51-Pad1)
- U24 pad 17: /soundbox/URT2_RX -> Net-(R52-Pad1)
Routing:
- net /soundbox/URT2_RX: track 10.9 -> 4.26 mm
- net Net-(R52-Pad1): track 0.00 -> 6.27 mm
- net /soundbox/URT2_TX: track 9.81 -> 4.70 mm
- net Net-(R51-Pad1): track 0.00 -> 4.47 mm

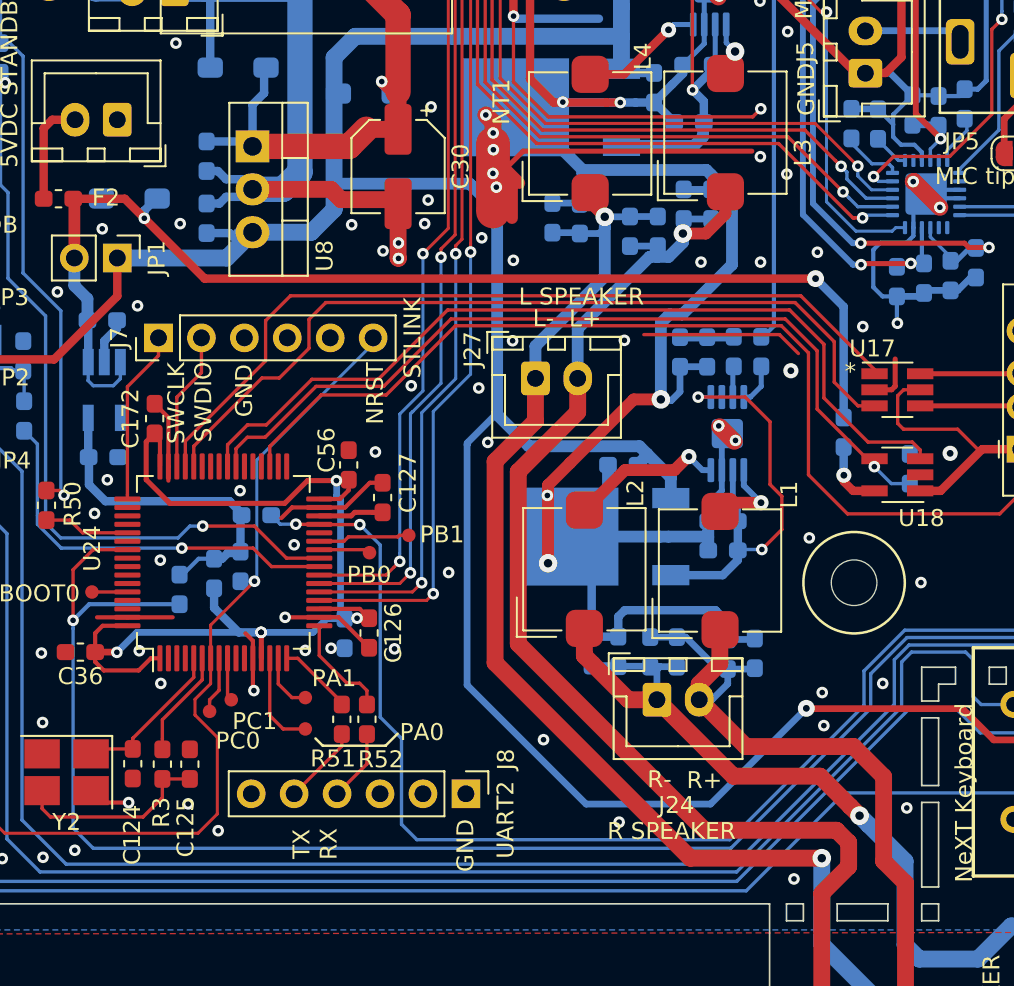
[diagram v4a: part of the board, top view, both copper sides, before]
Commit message: add BOOT1 pad
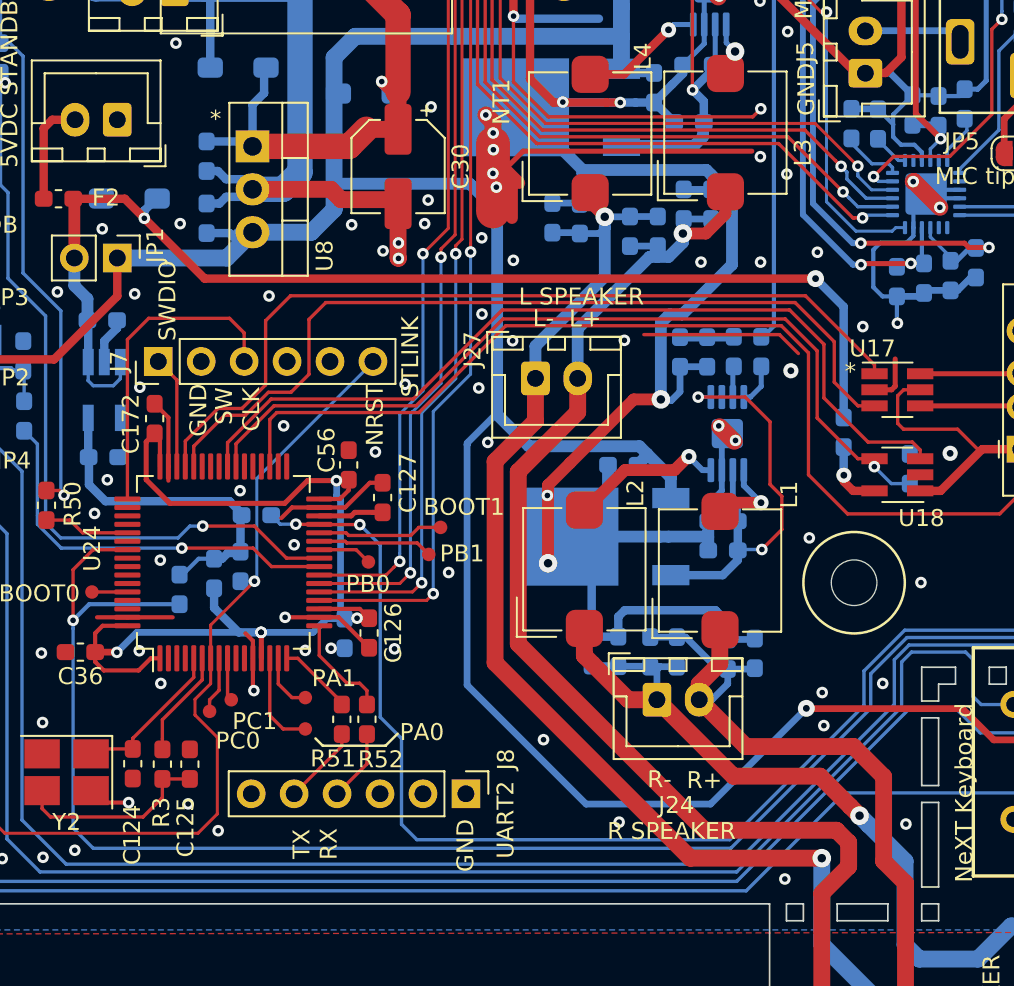
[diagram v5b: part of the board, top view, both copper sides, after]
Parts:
- added J30: BOOT1, custom_components:TestPad-D1.0mm, F.Cu at (86.2, 151.7)
- moved J23 1.63 mm to (85.5, 153.3)
- moved J7 1.40 mm to (69.5, 141.9)
- moved J22 0.55 mm to (82.0, 153.8)
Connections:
- J7 pad 1: /soundbox/SWCLK -> /soundbox/SWDIO
- J7 pad 2: /soundbox/SWDIO -> GND
- J7 pad 3: GND -> /soundbox/SWCLK
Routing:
- net /soundbox/SWCLK: track 10.3 -> 18.9 mm
- net Net-(J30-Pad1): track 0.00 -> 7.44 mm
- net /soundbox/SWDIO: track 8.21 -> 6.68 mm
- net /soundbox/NRST: track 74.4 -> 73.0 mm
- net Net-(J23-Pad1): track 5.44 -> 6.80 mm
- net Net-(U17-Pad1): track 49.3 -> 50.3 mm
- net Net-(R32-Pad2): track 79.3 -> 80.3 mm
- net Net-(U17-Pad3): track 49.9 -> 50.8 mm
- net GND: vias 367 -> 371
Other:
- board text added: "SW CLK"
- board text removed: "SWCLK"
